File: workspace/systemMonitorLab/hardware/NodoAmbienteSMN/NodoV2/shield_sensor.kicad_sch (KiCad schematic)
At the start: 7 parts, among them J4 Conn_01x01_Male, J5 Conn_01x01_Male, U2 AHT10, U3 DHT22, U4 Bmp280Module, U5 NodeMcuEsp8266

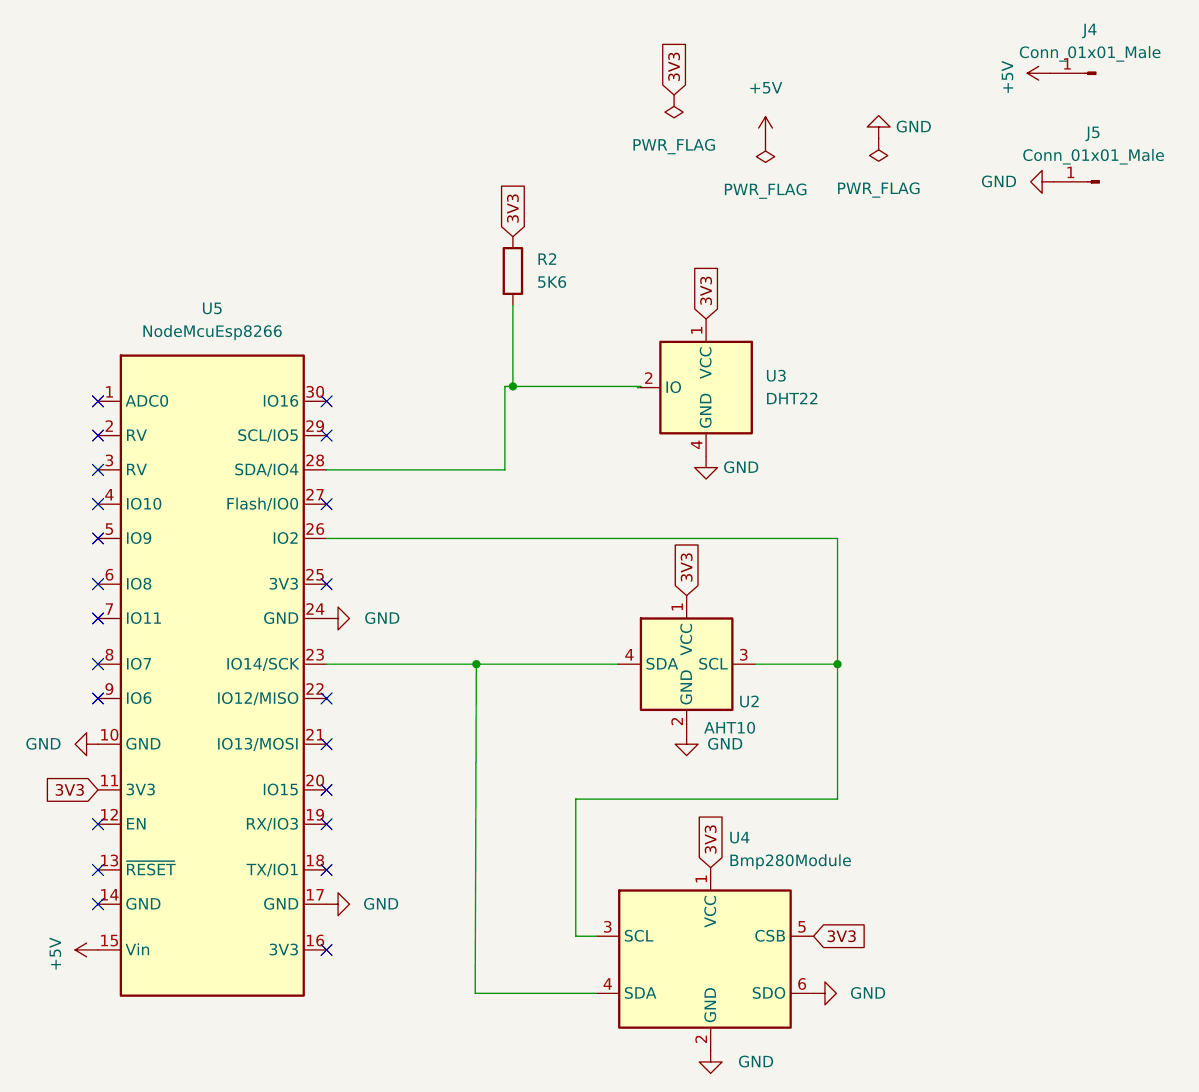
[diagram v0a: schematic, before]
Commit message: Se agregan leds de estado con sus respectivos conectores y se agrega en el codigo la configuracion de los GPIO para usar estos leds como indicadores de envio de datos, conexion con el servidor Web Socket y conectividad wifi
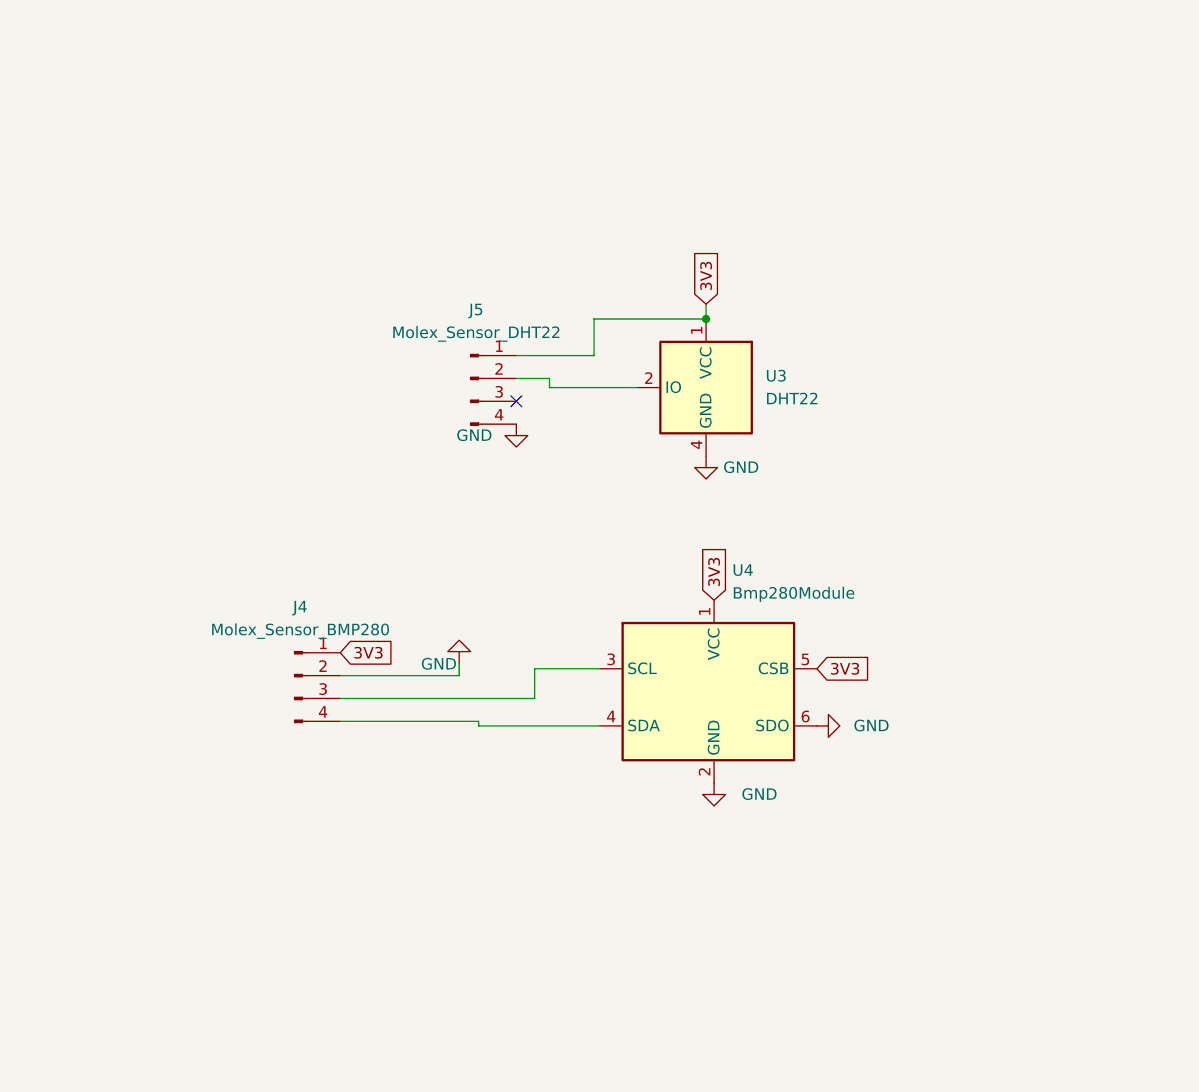
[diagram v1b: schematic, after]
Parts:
- removed J4, J5: Conn_01x01_Male, Connector_Pin:Pin_D1.0mm_L10.0mm, symbol Connector:Conn_01x01_Male
- removed R2: 5K6, Resistor_THT:R_Axial_DIN0207_L6.3mm_D2.5mm_P15.24mm_Horizontal, symbol Device:R
- removed U2: AHT10, Connector_PinHeader_2.54mm:PinHeader_1x04_P2.54mm_Vertical, symbol New_Library:AHT10
- removed U5: NodeMcuEsp8266, NodeMCU_Module:ESP8266, symbol New_Library:NodeMcuEsp8266
- added J4: Molex_Sensor_BMP280, Connector_PinHeader_2.54mm:PinHeader_1x04_P2.54mm_Horizontal, symbol Connector:Conn_01x04_Male
- added J5: Molex_Sensor_DHT22, Connector_PinHeader_2.54mm:PinHeader_1x04_P2.54mm_Horizontal, symbol Connector:Conn_01x04_Male
- U4: footprint Connector_PinHeader_2.54mm:PinHeader_1x06_P2.54mm_Vertical -> Modulos:BMP280_Module
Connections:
- net 3V3: now also J4.1 (Pin_1), J5.1 (Pin_1)
- net GND: now also J4.2 (Pin_2), J5.4 (Pin_4)
- net at U4.3 (SCL): now also J4.3 (Pin_3)
- net at U4.4 (SDA): now also J4.4 (Pin_4)
- net at U3.2 (IO): now also J5.2 (Pin_2)
- no-connect marks 22 -> 1
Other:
- moved on the sheet: U4
